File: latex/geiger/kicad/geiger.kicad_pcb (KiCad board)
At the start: 2 copper layers, 101.6 x 76.2 mm, 58 parts, among them P1 CONN_1, P2 CONN_1, Q1 NPN, Q10 NPN, Q11 NPN, Q12 NPN, Q2 NPN, Q3 NPN, Q4 NPN, Q5 NPN, Q6 NPN, Q7 NPN, Q8 NPN, Q9 NPN, T1 TRANSFO_2S

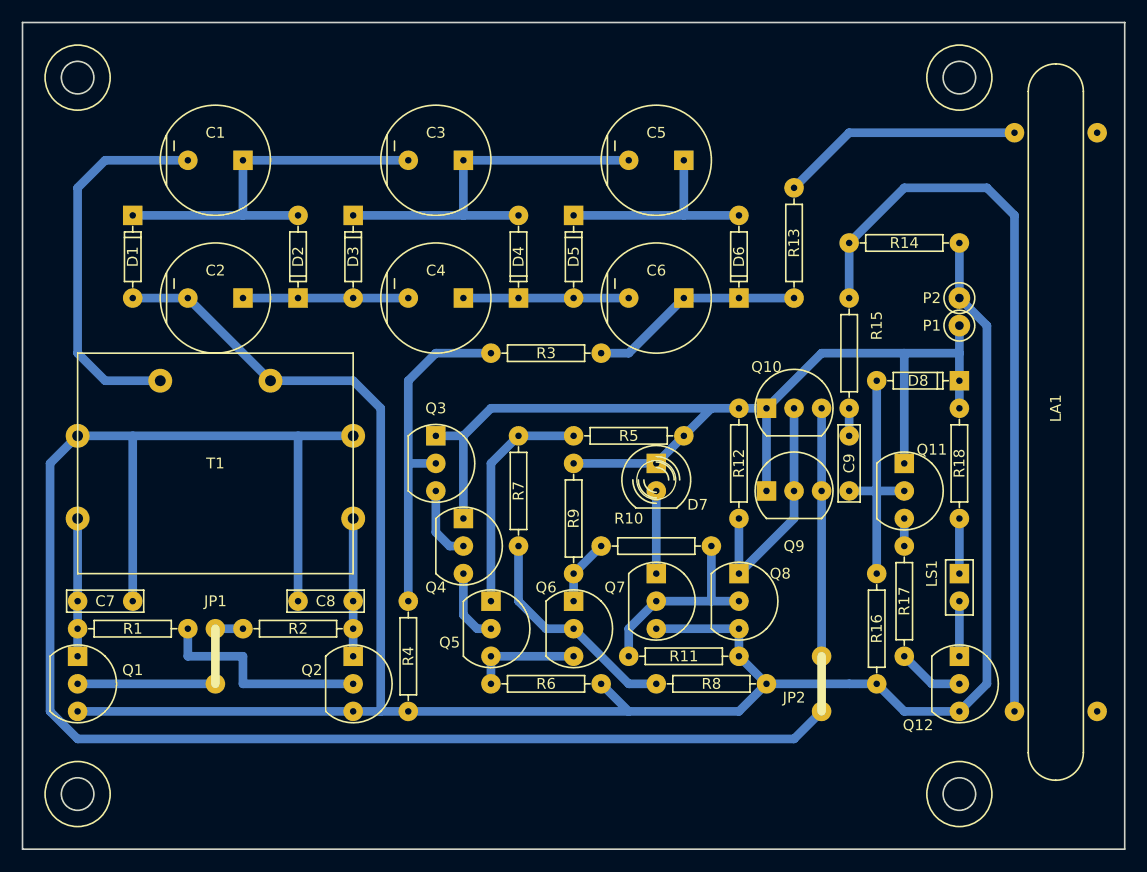
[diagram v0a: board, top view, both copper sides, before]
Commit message: add install-op-autowhite.sh
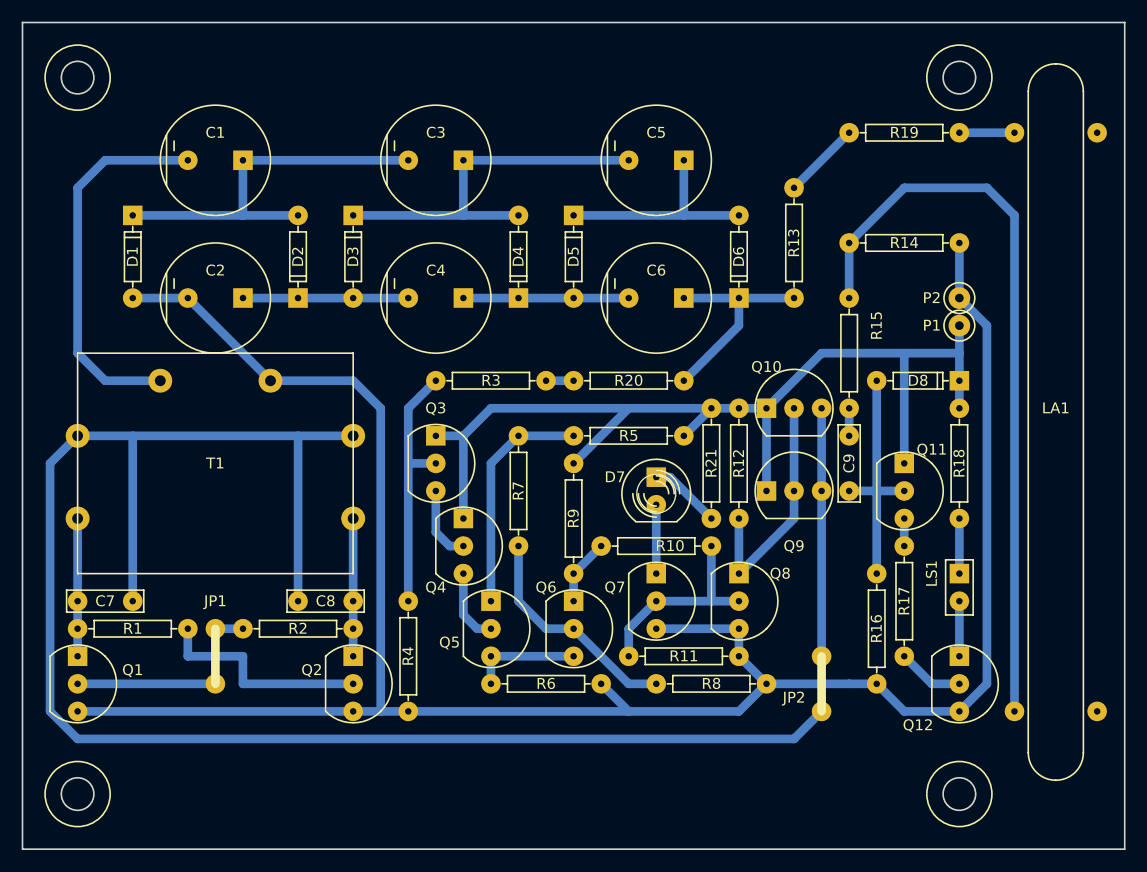
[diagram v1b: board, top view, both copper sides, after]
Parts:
- added R19: R, kicad:R4, F.Cu at (170.2, 58.4)
- added R20: R, kicad:R4, F.Cu at (144.8, 81.3)
- added R21: R, kicad:R4, F.Cu at (152.4, 88.9)
- moved R3 5.68 mm to (132.1, 81.3)
- moved D7 1.27 mm to (147.3, 91.4)
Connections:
- D8 pad 2: Net-(D7-Pad1) -> Net-(D8-Pad2)
- P1 pad 1: Net-(D7-Pad1) -> Net-(D8-Pad2)
- Q10 pad 1: Net-(D7-Pad1) -> Net-(D8-Pad2)
- Q11 pad 1: Net-(D7-Pad1) -> Net-(D8-Pad2)
- Q3 pad 1: Net-(D7-Pad1) -> Net-(D8-Pad2)
- Q4 pad 1: Net-(D7-Pad1) -> Net-(D8-Pad2)
- Q9 pad 1: Net-(D7-Pad1) -> Net-(D8-Pad2)
- R12 pad 1: Net-(D7-Pad1) -> Net-(D8-Pad2)
- R13 pad 1: Net-(LA1-Pad1) -> Net-(R13-Pad1)
- R18 pad 1: Net-(D7-Pad1) -> Net-(D8-Pad2)
- R3 pad 1: Net-(C6-Pad1) -> Net-(R20-Pad2)
- R5 pad 1: Net-(D7-Pad1) -> Net-(D8-Pad2)
- R9 pad 1: Net-(D7-Pad1) -> Net-(D8-Pad2)
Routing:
- net Net-(D8-Pad2): track 0.00 -> 95.2 mm
- net Net-(D7-Pad1): track 99.2 -> 6.66 mm
- net Net-(LA1-Pad1): track 22.4 -> 5.08 mm
- net Net-(Q3-Pad2): track 31.5 -> 23.9 mm
- net Net-(R13-Pad1): track 0.00 -> 7.18 mm
- net Net-(R20-Pad2): track 0.00 -> 2.54 mm
- net Net-(D7-Pad2): track 7.62 -> 6.35 mm
